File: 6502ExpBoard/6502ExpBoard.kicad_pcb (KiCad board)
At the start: 2 copper layers, 90.1 x 52.8 mm, 40 parts, among them J2 Expansion / Diag Port, U1 74LS373, U2 74LS373, U4 74LS373

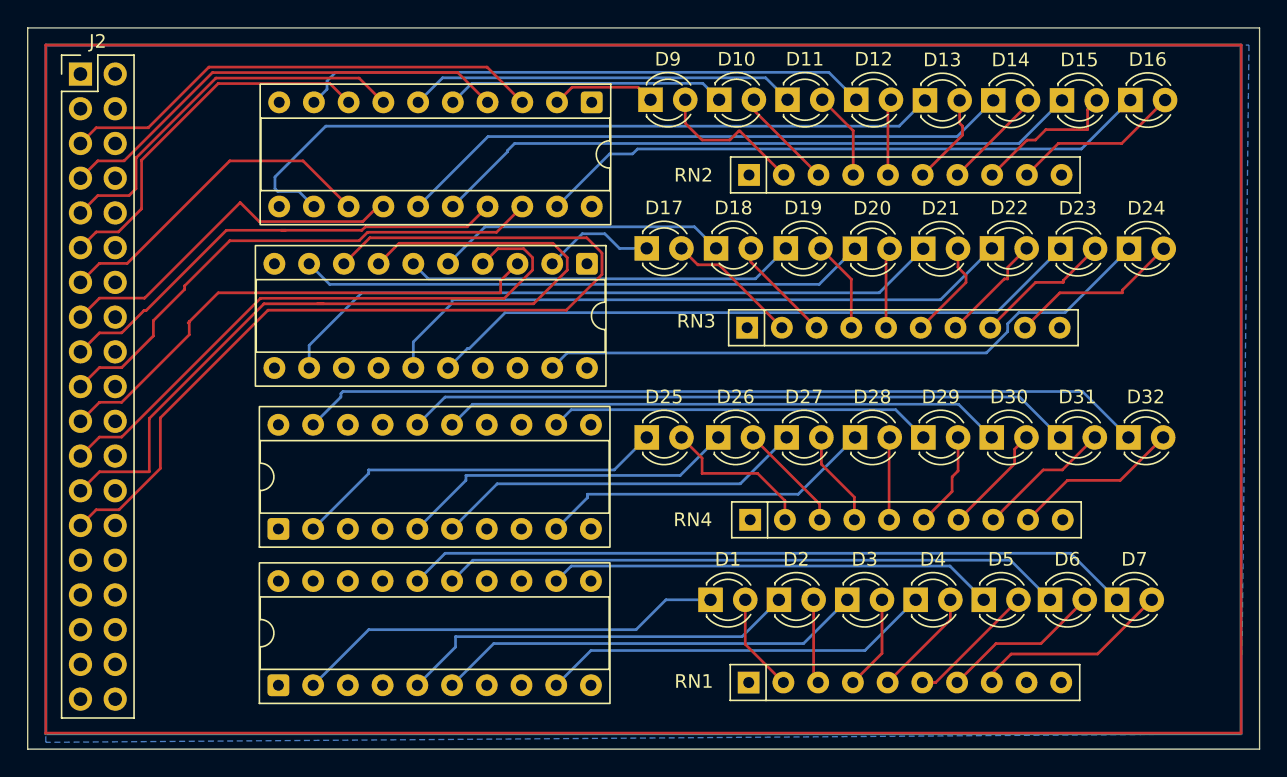
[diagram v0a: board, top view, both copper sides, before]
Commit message: Added Expansion
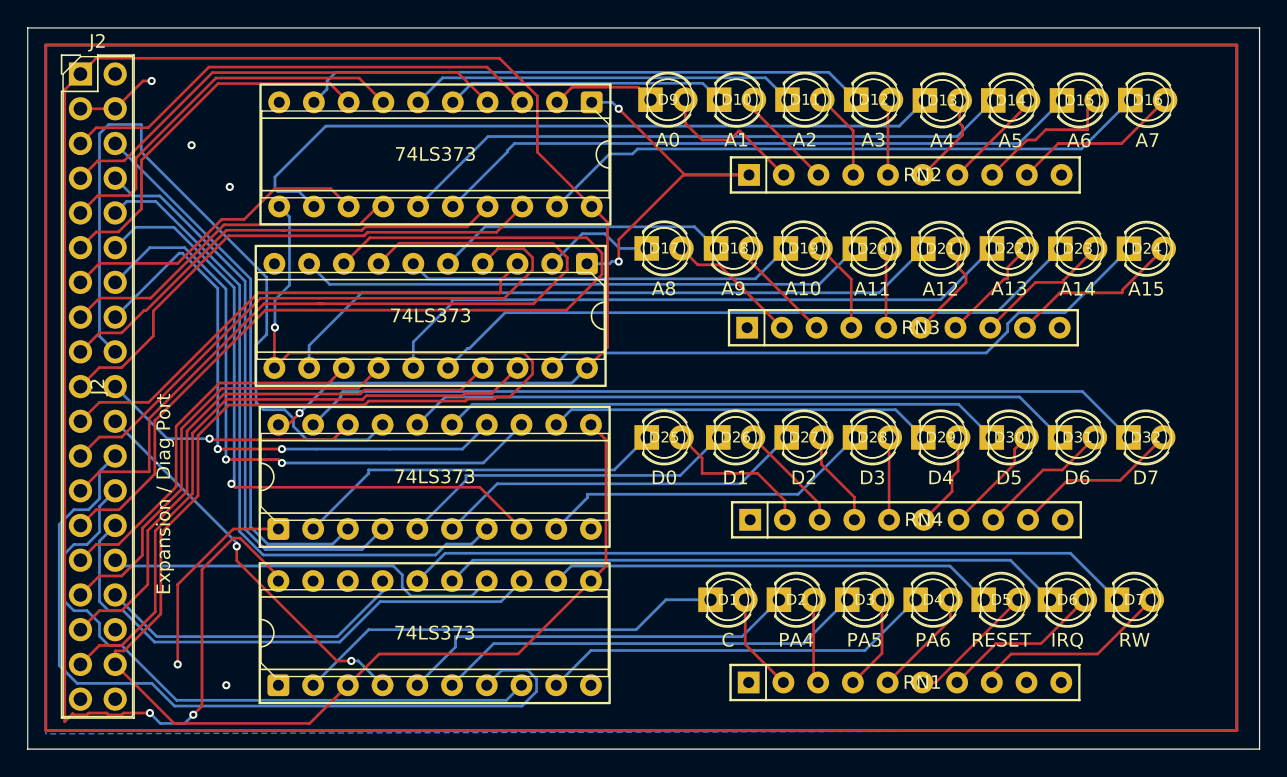
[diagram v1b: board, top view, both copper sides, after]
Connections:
- J2 pad 34: GND -> unconnected-(J2-Pin_34-Pad34)
- J2 pad 38: GND -> unconnected-(J2-Pin_38-Pad38)
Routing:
- net VCC: track 0.00 -> 159.2 mm, vias 0 -> 3
- net clock: track 0.00 -> 132.3 mm, vias 0 -> 1
- net PA5: track 0.00 -> 59.5 mm
- net D6: track 0.00 -> 55.4 mm
- net GND: track 0.00 -> 50.4 mm, vias 0 -> 7
- net D2: track 0.00 -> 49.6 mm
- net D3: track 0.00 -> 48.2 mm, vias 0 -> 1
- net PA6: track 0.00 -> 47.6 mm
- net A15: track 0.00 -> 47.0 mm
- net D4: track 0.00 -> 45.8 mm, vias 0 -> 2
- net D5: track 0.00 -> 42.7 mm, vias 0 -> 2
- net A14: track 0.00 -> 42.3 mm
- net D1: track 0.00 -> 42.1 mm
- net D0: track 0.00 -> 40.2 mm
- net Reset: track 0.00 -> 40.0 mm
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- added copper zone on F.Cu, net GND
